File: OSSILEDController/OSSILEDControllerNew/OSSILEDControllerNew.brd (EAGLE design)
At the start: 94 x 88 mm, 77 parts, among them Q1 NX-3215, U1 OPA2347, U2 MSP430F2132, U3 LM7321, U4 MAX1682, U5 MAX890L, U6 MAX4376, U7 TPS3838, U8 MCP1700_SOT23, X1 ESQ-126-38-G-D, X2 5268-03, X3 ICCON_POWERCON, X4 ICCON_POWERCON, X5 WEIDMULLER, X6 JTAG10PINMINI-H, X7 5268-03

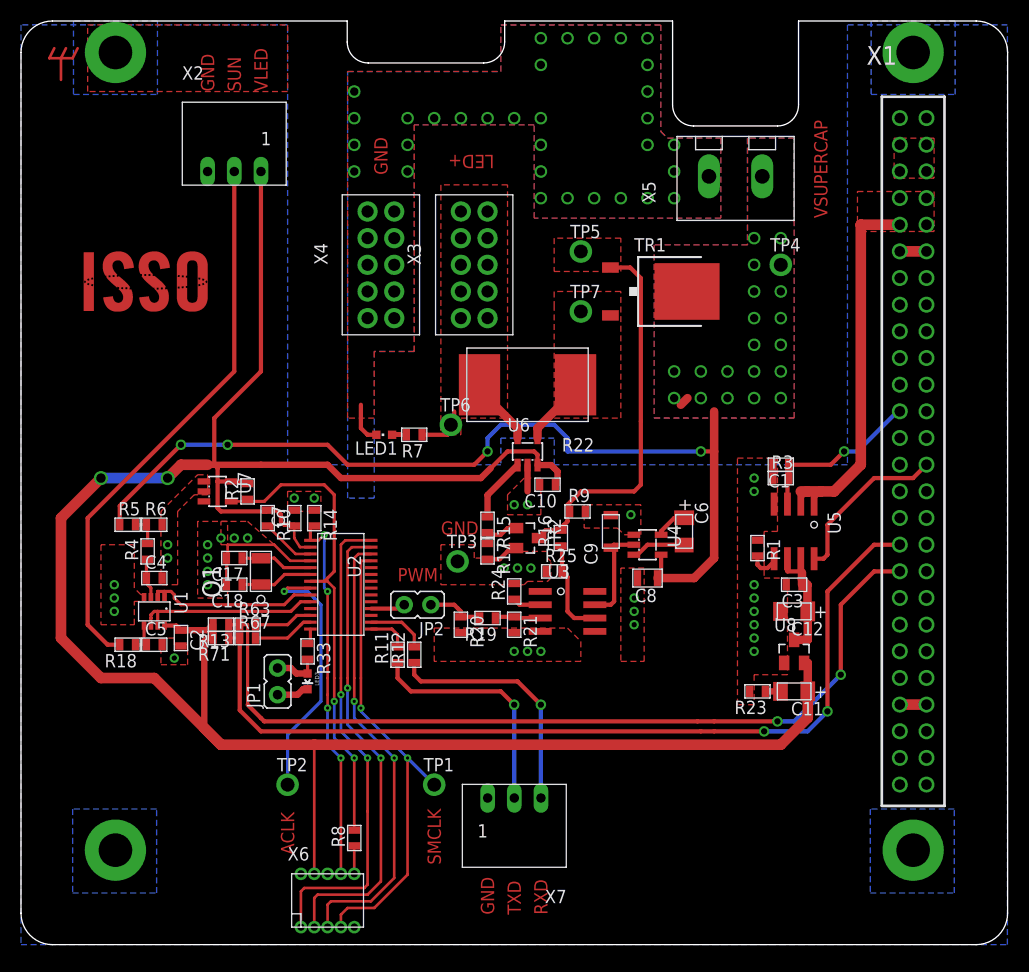
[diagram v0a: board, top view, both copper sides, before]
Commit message: gerber files are created / led current setting fixed to 9.7A
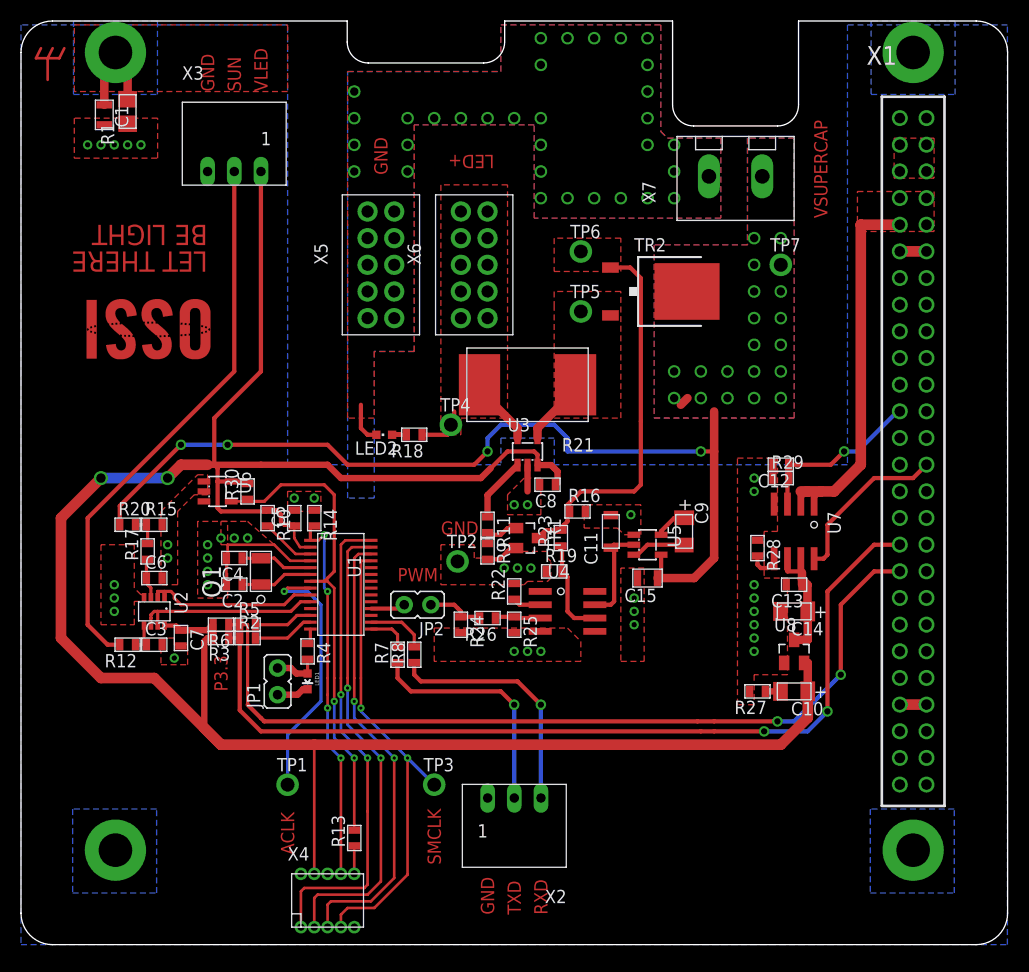
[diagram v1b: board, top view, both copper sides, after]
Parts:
- removed C17, C18: 12.5pF, OSSI:C0603(1608)
- removed LED3: (no value), SparkFun:LED-0603
- removed R33: 1k, OSSI:R0603(1608)
- removed R63, R67: 250, OSSI:R0603(1608)
- removed R71: 10k, OSSI:R0603(1608)
- removed U$1: OSSILOGORECT, OSSI:OSSILOGORECT1005
- added C13: 100nF, OSSI:C0603(1608)
- added C14: 10uF, LDO Tantal 16V, OSSI:C1206(3216)-A
- added C15: 1uF 0805, OSSI:C0805(2012)
- added LED2: (no value), led:CHIPLED_0603
- added R26: 1.5k, OSSI:R0603(1608)
- added R27: 0, OSSI:R0603(1608)
- added R28: TBD, OSSI:R0603(1608)
- added R29, R30: 100k, OSSI:R0603(1608)
- added U$: OSSILOGORECT, OSSI:OSSILOGORECT1005
- C1: value 1uF -> (none); device OSSI:C0603(1608) -> OSSI:C0805(2012)
- C10: value 100nF -> 10uF, LDO Tantal 16V; device OSSI:C0603(1608) -> OSSI:C1206(3216)-A
- C11: value 10uF, LDO Tantal 16V -> 1206 Cap; device OSSI:C1206(3216)-A -> OSSI:C1206-GCM31
- C12: value 10uF, LDO Tantal 16V -> 1uF; device OSSI:C1206(3216)-A -> OSSI:C0603(1608)
- C2, C4: value 100nF -> 12.5pF
- C6: value 10uF, LDO Tantal 16V -> 100nF; device OSSI:C1206(3216)-A -> OSSI:C0603(1608)
- C8: value 1uF 0805 -> 100nF; device OSSI:C0805(2012) -> OSSI:C0603(1608)
- C9: value 1206 Cap -> 10uF, LDO Tantal 16V; device OSSI:C1206-GCM31 -> OSSI:C1206(3216)-A
- LED1: device led:CHIPLED_0603 -> SparkFun:LED-0603
- R1: value TBD -> 511; device OSSI:R0603(1608) -> OSSI:WSL1206
- R11: value 4.7k -> 9.1k
- R12: value 4.7k -> 1k
- R13: value 10k -> 4.7k
- R15, R20: value (none) -> 100k
- R16: value 100k -> DNP
- R17: value (none) -> 1k
- R18: value 1k -> 1.5k
- R19: value (none) -> 2.2k
- R2, R5: value 100k -> 250
- R21: value (none) -> 0.005, 2W RSENSE; device OSSI:R0603(1608) -> OSSI:R4527(12070)
- R22: value 0.005, 2W RSENSE -> 1.1k; device OSSI:R4527(12070) -> OSSI:R0603(1608)
- R23: value 0 -> 100k
- R24: value 1.1k -> 100k
- R25: value 2.2k -> (none)
- R3, R6: value 100k -> 10k
- R7: value 1.5k -> 4.7k
- R9: value DNP -> 6.2k
- TR1: value FDD8896 -> FDV301N; device OSSI:TO252 -> OSSI:SOT23
- TR2: value FDV301N -> FDD8896; device OSSI:SOT23 -> OSSI:TO252
- U1: value OPA2347 -> MSP430F2132; device OSSI:SOT23-8DCN -> OSSI:PW28
- U2: value MSP430F2132 -> OPA2347; device OSSI:PW28 -> OSSI:SOT23-8DCN
- U3: value LM7321 -> MAX4376; device OSSI:SO8 -> OSSI:SOT23-5DBV
- U4: value MAX1682 -> LM7321; device OSSI:SOT23-5DBV -> OSSI:SO8
- U5: value MAX890L -> MAX1682; device OSSI:SO8 -> OSSI:SOT23-5DBV
- U6: value MAX4376 -> TPS3838
- U7: value TPS3838 -> MAX890L; device OSSI:SOT23-5DBV -> OSSI:SO8
- X3: value ICCON_POWERCON -> 5268-03; device OSSI:ICCON6643220-1 -> OSSI:5268-03
- X4: value ICCON_POWERCON -> JTAG10PINMINI-H; device OSSI:ICCON6643220-1 -> OSSI:M50-3200545
- X5: value WEIDMULLER -> ICCON_POWERCON; device OSSI:WEIDMULLER1760490000 -> OSSI:ICCON6643220-1
- X6: value JTAG10PINMINI-H -> ICCON_POWERCON; device OSSI:M50-3200545 -> OSSI:ICCON6643220-1
- X7: value 5268-03 -> WEIDMULLER; device OSSI:5268-03 -> OSSI:WEIDMULLER1760490000
- moved H1 76.0 mm to (9.00, 9.00)
- moved H2 76.0 mm to (85.0, 9.00)
- moved H3 76.0 mm to (85.0, 85.0)
- moved H4 76.0 mm to (9.00, 85.0)
- moved R1 73.0 mm to (10.2, 79.4), turned to 90 degrees
- moved C1 72.6 mm to (7.94, 79.1), turned to 270 degrees
- moved X2 65.4 mm to (47.0, 14.0), turned to 180 degrees
- moved X7 62.9 mm to (68.1, 73.2), turned to 0 degrees
- moved X6 62.2 mm to (43.2, 64.8)
- moved C3 61.2 mm to (12.7, 28.6), turned to 0 degrees
- moved X4 60.8 mm to (29.2, 4.21)
- moved R3 55.5 mm to (19.1, 29.2), turned to 180 degrees
- moved U7 55.1 mm to (73.7, 39.4), turned to 180 degrees
- moved C6 50.7 mm to (12.7, 34.9), turned to 0 degrees
- moved TP4 34.9 mm to (41.0, 49.5)
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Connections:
- net 3.3VLED: now also C5.1, C8.1, R3.2, R30.2, R6.2, U1.2, U2.8, U3.3, U6.5, X3.1, X4.4; no longer C11.1, C2.1, R13.2, R2.2, R71.2, U1.8, U2.2, U6.3, U7.5, X2.1, X6.4
- net ACLK_OUT: now also TP1.TP, U1.8; no longer TP2.TP, U2.8
- net ADC1: now also U1.9, U2.1, U2.2; no longer U1.1, U1.2, U2.9
- net ADC2: now also U1.10, U2.6, U2.7; no longer U1.6, U1.7, U2.10
- net GND: now also C11.P$2, C13.2, C14.2, C15.2, C6.2, LED2.C, R1.P$1, R15.2, R16.2, R19.1, R22.2, R25.2, R27.2, R28.1, R29.1, TP2.TP, TR1.2, U3.2, U4.4, U5.1, U6.1, U7.4, X2.1, X3.3, X5.1, X5.10, X5.3, X5.4, X5.5, X5.6, X5.7, X5.8, X5.9, X7.2; no longer C10.2, C17.2, C18.2, C9.P$2, LED3.C, R1.1, R17.2, R20.2, R21.2, R23.2, R25.1, R3.1, R6.2, TP3.TP, TR2.2, U3.4, U4.1, U5.4, U7.1, U7.2, X2.3, X4.1, X4.10, X4.2, X4.3, X4.4, X4.5, X4.6, X4.7, X4.8, X6.9, X7.1
- net LED_-FAULT: now also U7.8; no longer U5.8
- net LED_OFF: now also C12.1, R29.2, U7.3; no longer C1.1, R3.2, U5.3
- net LED_SCL: now also R2.1, R3.1; no longer R67.1, R71.1
- net LED_SDA: now also R5.1, R6.1; no longer R13.1, R63.1
- net N$10: now also R28.2, U7.5; no longer R1.2, U5.5
- net N$11: now also R15.1, R17.2, R20.2; no longer R4.2, R5.2, R6.1
- net N$12: now also R18.1, R21.P$2, TP4.TP, U3.5, X6.1, X6.10, X6.2, X6.3, X6.4, X6.5, X6.6, X6.7, X6.8, X6.9; no longer R22.P$2, R7.1, TP6.TP, U6.5, X3.1, X3.10, X3.2, X3.3, X3.4, X3.5, X3.6, X3.7, X3.8, X3.9
- net N$13: now also C11.P$1, U4.7, U5.2; no longer C9.P$1, U3.7, U4.2
- net N$14: now also R19.2, R23.1, U4.6; no longer R16.1, R25.2, U3.6
- net N$15: now also U1.27, X4.3; no longer U2.27, X6.3
- net N$16: now also R21.P$1, TP5.TP, TR2.S, U3.4; no longer R22.P$1, TP7.TP, TR1.S, U6.4
- net N$17: now also C10.2, R27.1; no longer C11.2, R23.1
- net N$18: now also R22.1, U4.2; no longer R24.1, U3.2
- net N$19: now also C4.1, U1.5; no longer C17.1, U2.5
- net N$20: now also C2.1, U1.6; no longer C18.1, U2.6
- net N$21: now also LED1.A, R4.2; no longer LED3.A, R33.2
- net N$22: now also R5.2, U1.12; no longer R63.2, U2.12
- net N$23: now also R2.2, U1.13; no longer R67.2, U2.13
- net N$24: now also R11.1, U3.1; no longer R15.1, U6.1
- net N$25: now also R4.1, U1.14; no longer R33.1, U2.14
- net N$26: now also C9.2, U5.3; no longer C6.2, U4.3
- net N$27: now also C9.1, U5.5; no longer C6.1, U4.5
- net N$28: now also R8.2, U1.16; no longer R12.2, U2.16
- net N$29: now also LED2.A, R18.2; no longer LED1.A, R7.2
- net N$3: now also U1.28, X4.1; no longer U2.28, X6.1
- net N$30: now also R11.2, R9.1, TR1.1; no longer R15.2, R17.1, TR2.1
- net N$31: now also U1.26, X4.5; no longer U2.26, X6.5
- net N$32: now also R13.1, X4.10; no longer R8.1, X6.10
- net N$33: now also U1.18; no longer U2.18
- net N$39: now also R7.2, U1.15; no longer R11.2, U2.15
- net N$4: now also U1.3; no longer U2.3
- net N$5: now also C13.1, C14.1, U7.6, U7.7; no longer C12.1, C3.1, U5.6, U5.7
- net N$6: now also R16.1, R23.2, TP6.TP, TR1.3, TR2.G; no longer R16.2, R9.1, TP5.TP, TR1.G, TR2.3
- net N$7: now also C6.1, R17.1, U2.3; no longer C4.1, R4.1, U1.3
- net N$8: now also C3.1, R12.1, U2.5; no longer C5.1, R18.1, U1.5
- net N$9: now also R25.1, R26.1, U4.3; no longer R19.1, R21.1, U3.3
- net PWM: now also R24.1, R26.2; no longer R19.2, R20.1
- net RESET_LED: now also R13.2, R30.1, U1.7, U6.4; no longer R2.1, R8.2, U2.7, U7.4
- net RXD: now also R8.1, X2.3; no longer R12.1, X7.3
- net SMCLK_OUT: now also TP3.TP, U1.25, X4.7; no longer TP1.TP, U2.25, X6.7
- net STRUT_GND: now also C1.1, H4.B3,2, R1.P$2; no longer H1.B3,2
- net SUN: now also R12.2, X3.2; no longer R18.2, X2.2
- net TEST: now also U1.1, X4.8; no longer U2.1, X6.8
- net TXD: now also R7.1, X2.2; no longer R11.1, X7.2
- net VBUS: now also U7.1, U7.2; no longer U5.1, U5.2
- net VSUPERCAP: now also C15.1, R20.1, TP7.TP, TR2.D, U5.4, X7.1; no longer C8.1, R5.1, TP4.TP, TR1.D, U4.4, X5.1
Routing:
- net STRUT_GND: track 0.00 -> 7.41 mm
- net GND: vias 67 -> 72
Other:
- board text added: "BE LIGHT"
- board text added: "LET THERE"
- board text added: "P3.3"

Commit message: beta 1 release
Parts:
- added X8: (no value), OSSI:1X03
- moved R11 5.08 mm to (44.5, 34.9)
- moved R15 5.08 mm to (12.7, 34.9)
- moved R17 5.08 mm to (12.1, 32.4)
- moved R20 5.08 mm to (10.2, 34.9)
- moved R21 5.08 mm to (48.3, 48.3)
- moved R29 5.08 mm to (72.4, 39.4)
- moved R9 5.08 mm to (44.5, 32.4)
- moved U3 5.08 mm to (48.3, 41.9)
- moved C7 5.08 mm to (15.2, 24.1)
- moved Q1 5.08 mm to (22.9, 30.5)
- moved R19 5.08 mm to (50.8, 30.5)
- moved R2 5.08 mm to (21.6, 24.1)
- moved R22 5.08 mm to (47.0, 28.6)
- moved R24 5.08 mm to (41.9, 25.4)
- moved R25 5.08 mm to (47.0, 25.4)
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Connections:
- net GND: now also X8.3
- net LED_SCL: now also X8.2
- net LED_SDA: now also X8.1
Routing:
- net LED_SDA: track 82.0 -> 94.1 mm
- net LED_SCL: track 85.9 -> 97.5 mm
- net LED_OFF: track 16.7 -> 22.8 mm
- net LED_-FAULT: track 16.1 -> 21.2 mm
- net TEST: track 36.5 -> 31.4 mm
- net N$3: track 46.7 -> 41.6 mm
- net N$15: track 45.0 -> 39.9 mm
- net SUN: track 52.8 -> 57.9 mm
- net SMCLK_OUT: track 45.4 -> 40.3 mm
- net RESET_LED: track 46.2 -> 41.1 mm
- net N$31: track 43.4 -> 38.3 mm
- net N$6: track 36.8 -> 41.8 mm
- net VBUS: track 36.3 -> 41.3 mm
- net TXD: track 22.5 -> 21.3 mm
- net RXD: track 23.3 -> 22.0 mm
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- added copper zone on layer 16, net N$12
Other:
- outline, holes or cut-outs redrawn
- board text added: "SCL"
- board text added: "SDA"
- board text added: "VBUS"
